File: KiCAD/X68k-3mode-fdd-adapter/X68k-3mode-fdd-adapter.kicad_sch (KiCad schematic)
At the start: 79 parts, among them J101 4pin, J102 Conn_02x06_Odd_Even, J103 Conn_01x02, J104 Conn_01x04, J105 Conn_01x02, J106 Conn_02x17_Odd_Even, J107 Conn_02x17_Odd_Even, J108 Conn_02x17_Odd_Even, Q101 DTC143Z, Q102 2SC2712, SW101 SW_DIP_x04, SW102 RESET, U101 INA3221AIRGVR, U102 SLG46826G(V2), U103 SLG46826G(V2), U104 CH32X035C8T6, U105 SLG46826G(V2)

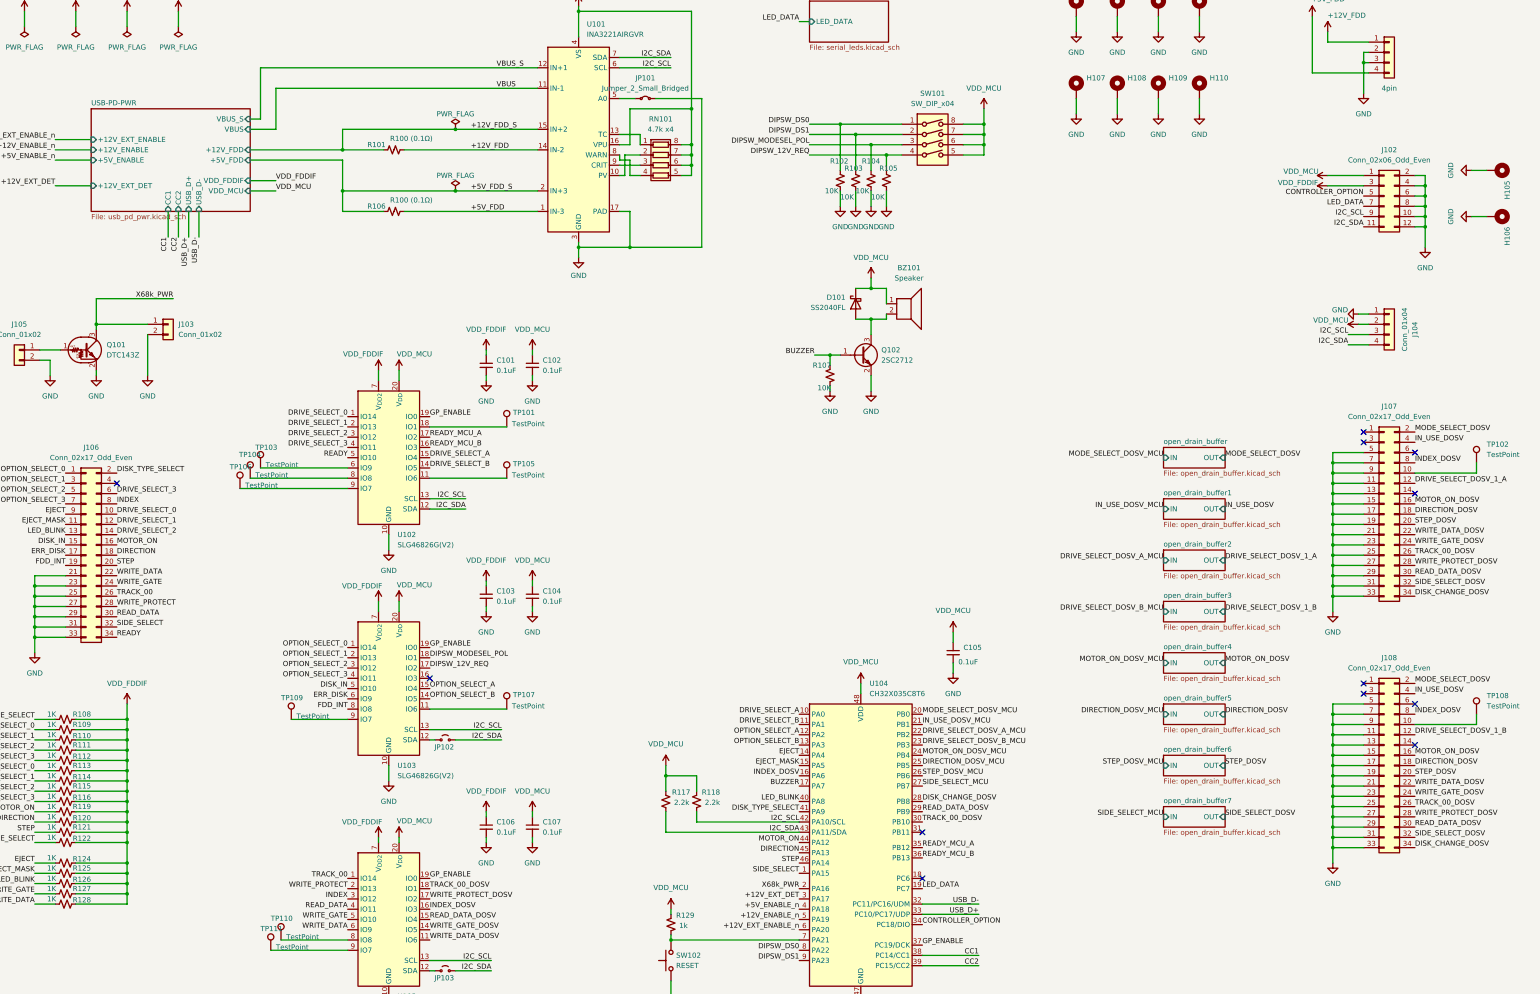
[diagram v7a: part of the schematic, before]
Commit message: シルクをさらに調整
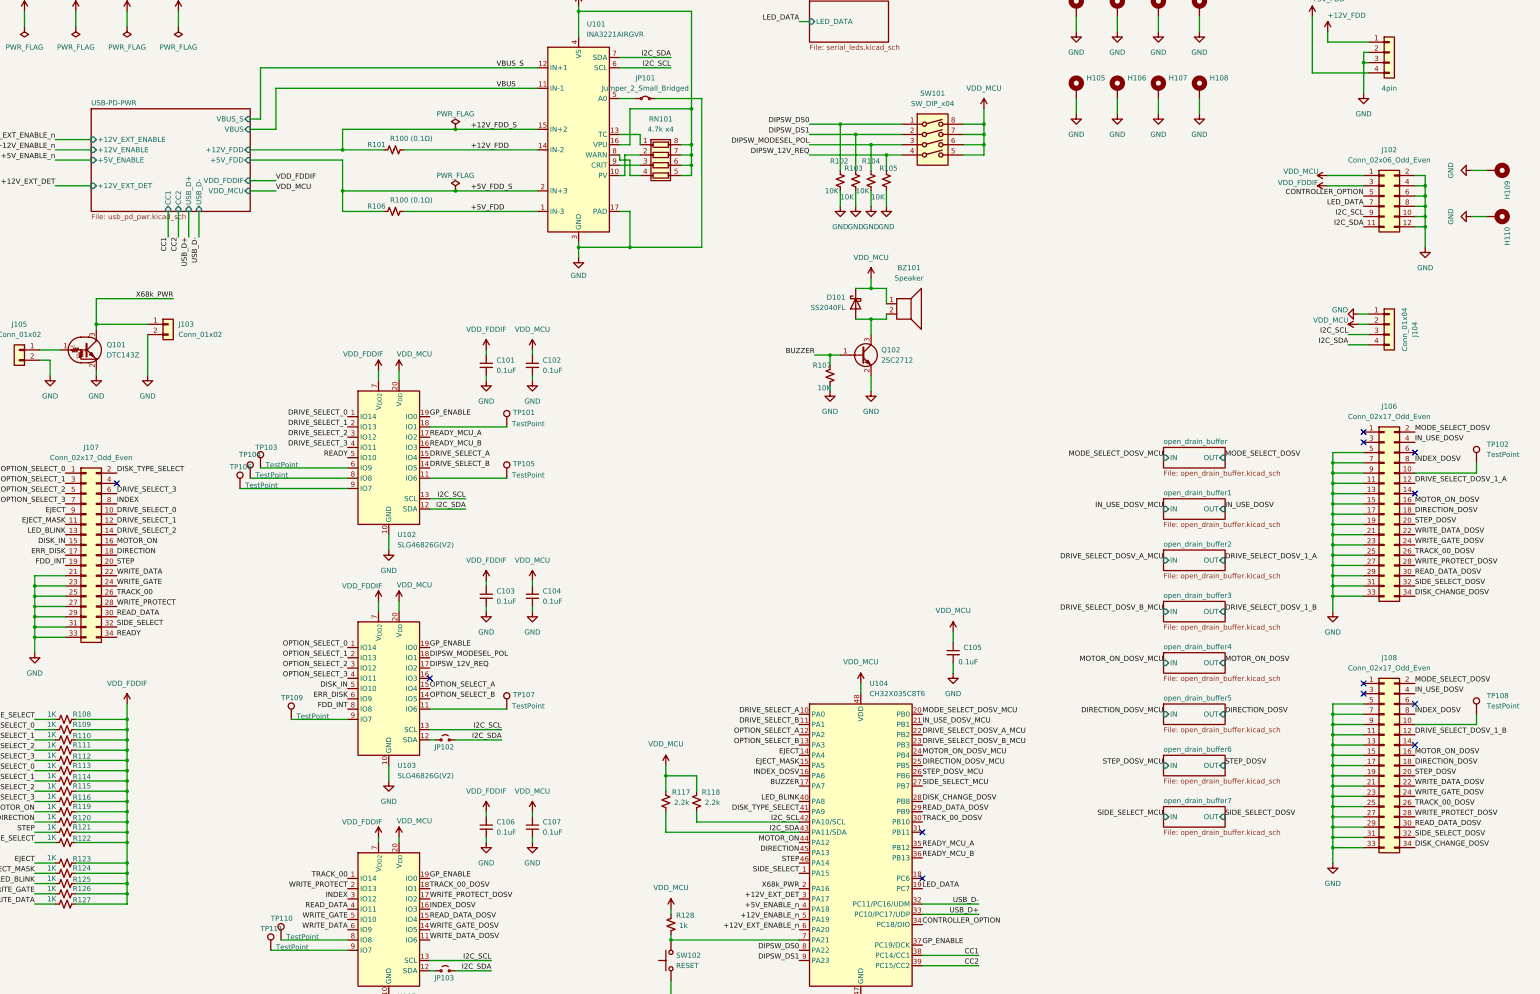
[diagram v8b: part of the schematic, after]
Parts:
- U104: footprint Package_QFP:LQFP-48-1EP_7x7mm_P0.5mm_EP3.6x3.6mm_ThermalVias -> Package_QFP:LQFP-48_7x7mm_P0.5mm
- renumbered H107 to H105, H108 to H106, H109 to H107, H110 to H108, H105 to H109, H106 to H110, J107 to J106, J106 to J107, R124 to R123, R125 to R124, R126 to R125, R127 to R126, R128 to R127, R129 to R128
